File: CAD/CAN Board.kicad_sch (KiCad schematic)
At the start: 40 parts, among them J1 Conn_01x04, J10 Conn_01x03, J11 Conn_01x03, J2 Conn_01x06, J3 USB_C_Receptacle_USB2.0_16P, J4 Conn_01x02, J5 Conn_01x02, J6 Conn_01x02, J7 Conn_01x02, J8 Conn_01x02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

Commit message: updated baord
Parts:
- C1, C2: value 27p -> 15p
- Y1: value Crystal_GND24 -> 12MHz
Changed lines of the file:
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@@
 	(label "QSPI_SCLK"
 		(at 149.225 83.185 0)
-		(fields_autoplaced yes)
 		(effects
 			(font
@@
 	(label "QSPI_SD1"
 		(at 15.24 83.82 0)
-		(fields_autoplaced yes)
 		(effects
 			(font
@@
 	(label "QSPI_SS"
 		(at 149.225 80.01 0)
-		(fields_autoplaced yes)
 		(effects
 			(font
@@
 	(label "XOUT"
 		(at 15.24 116.84 0)
-		(fields_autoplaced yes)
 		(effects
 			(font
@@
 	(label "QSPI_SD3"
 		(at 15.24 88.9 0)
-		(fields_autoplaced yes)
 		(effects
 			(font
@@
 	(label "QSPI_SD0"
 		(at 195.58 75.565 180)
-		(fields_autoplaced yes)
 		(effects
 			(font
@@
 	(label "QSPI_SD2"
 		(at 195.58 83.185 180)
-		(fields_autoplaced yes)
 		(effects
 			(font
@@
 	(label "QSPI_SD2"
 		(at 15.24 86.36 0)
-		(fields_autoplaced yes)
 		(effects
 			(font
@@
 	(label "QSPI_SD3"
 		(at 195.58 85.725 180)
-		(fields_autoplaced yes)
 		(effects
 			(font
@@
 	(label "ucd+"
 		(at 90.17 66.04 0)
-		(fields_autoplaced yes)
 		(effects
 			(font
@@
 	(label "QSPI_SCLK"
 		(at 15.24 92.71 0)
-		(fields_autoplaced yes)
 		(effects
 			(font
@@
 	(label "XOUT"
 		(at 46.99 33.02 180)
-		(fields_autoplaced yes)
 		(effects
 			(font
@@
 	(label "XIN"
 		(at 15.24 111.76 0)
-		(fields_autoplaced yes)
 		(effects
 			(font
@@
 	(label "ucd-"
 		(at 90.17 68.58 0)
-		(fields_autoplaced yes)
 		(effects
 			(font
@@
 	(label "QSPI_SS"
 		(at 15.24 77.47 0)
-		(fields_autoplaced yes)
 		(effects
 			(font
@@
 	(label "QSPI_SD0"
 		(at 15.24 81.28 0)
-		(fields_autoplaced yes)
 		(effects
 			(font
@@
 	(label "QSPI_SD1"
 		(at 195.58 78.105 180)
-		(fields_autoplaced yes)
 		(effects
 			(font
@@
 	(label "XIN"
 		(at 45.72 22.86 180)
-		(fields_autoplaced yes)
 		(effects
 			(font
@@
 			)
 		)
-		(property "Value" "27p"
+		(property "Value" "15p"
 			(at 20.447 35.941 0)
 			(effects
@@
 			)
 		)
-		(property "Value" "27p"
+		(property "Value" "15p"
 			(at 20.447 25.781 0)
 			(effects
@@
 			)
 		)
-		(property "Value" "Crystal_GND24"
+		(property "Value" "12MHz"
 			(at 41.91 25.781 90)
 			(effects
@@
 			)
 		)
-		(property "Datasheet" "~"
+		(property "Datasheet" "Abracon ABM8-272-T3"
 			(at 29.21 27.94 0)
 			(effects

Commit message: added LED and cleanup
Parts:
- removed J1: Conn_01x04, Connector_Molex:Molex_PicoBlade_53047-0410_1x04_P1.25mm_Vertical, symbol Connector_Generic:Conn_01x04
- removed J10: Conn_01x03, Connector_Molex:Molex_PicoBlade_53047-0310_1x03_P1.25mm_Vertical, symbol Connector_Generic:Conn_01x03
- removed J2: Conn_01x06, Connector_Molex:Molex_PicoBlade_53047-0610_1x06_P1.25mm_Vertical, symbol Connector_Generic:Conn_01x06
- added D1: LED, LED_SMD:LED_0603_1608Metric_Pad1.05x0.95mm_HandSolder, symbol Device:LED
- added J1, J12: Conn_01x03, Connector_Molex:Molex_PicoBlade_53047-0310_1x03_P1.25mm_Vertical, symbol Connector_Generic:Conn_01x03
- added J10: Conn_01x02, Connector_Molex:Molex_PicoBlade_53047-0210_1x02_P1.25mm_Vertical, symbol Connector_Generic:Conn_01x02
- added J2: Conn_01x04, Connector_Molex:Molex_PicoBlade_53047-0410_1x04_P1.25mm_Vertical, symbol Connector_Generic:Conn_01x04
- added Q1: NMOS, Package_TO_SOT_SMD:SOT-323_SC-70, symbol Simulation_SPICE:NMOS
- added R19: 1k, Resistor_SMD:R_0603_1608Metric_Pad0.98x0.95mm_HandSolder, symbol Device:R
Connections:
- net +3V3: now also D1.2 (A), J12.2 (Pin_2)
- net +5V: now also J12.1 (Pin_1)
- net ADC 0: now also J1.2 (Pin_2)
- net ADC 1: now also J1.3 (Pin_3)
- net GND: now also J12.3 (Pin_3), Q1.3 (S)
- net GPIO 15: now also J1.1 (Pin_1), Q1.2 (G)
- net RX0: now also J10.2 (Pin_2)
- net SPI1 CSn: now also J2.3 (Pin_3)
- net SPI1 RX: now also J2.2 (Pin_2)
- net SPI1 SCK: now also J2.4 (Pin_4)
- net SPI1 TX: now also J2.1 (Pin_1)
- net TX0: now also J10.1 (Pin_1)
- new net: D1.1 (K), R19.1
- new net: Q1.1 (D), R19.2
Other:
- moved on the sheet: J11

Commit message: updated board
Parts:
- added R20: 220, Resistor_SMD:R_0603_1608Metric_Pad0.98x0.95mm_HandSolder, symbol Device:R
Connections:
- net GPIO 15: now also R20.1; no longer Q1.2 (G)
- new net: Q1.2 (G), R20.2
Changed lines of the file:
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@@
 	(global_label "GPIO 15"
 		(shape bidirectional)
-		(at 214.63 77.47 180)
+		(at 214.63 69.85 180)
 		(fields_autoplaced yes)
 		(effects
@@
 		)
 		(property "Intersheetrefs" "${INTERSHEET_REFS}"
-			(at 202.6716 77.47 0)
+			(at 202.6716 69.85 0)
 			(effects
 				(font
@@
 					(unit 1)
 				)
+			)
+		)
+	)
+	(symbol
+		(lib_id "Device:R")
+		(at 214.63 73.66 0)
+		(unit 1)
+		(exclude_from_sim no)
+		(in_bom yes)
+		(on_board yes)
+		(dnp no)
+		(fields_autoplaced yes)
+		(property "Reference" "R20"
+			(at 217.17 72.3899 0)
+			(effects
+				(font
+					(size 1.27 1.27)
+				)
+				(justify left)
+			)
+		)
+		(property "Value" "220"
+			(at 217.17 74.9299 0)
+			(effects
+				(font
+					(size 1.27 1.27)
+				)
+				(justify left)
+			)
+		)
+		(property "Footprint" "Resistor_SMD:R_0603_1608Metric_Pad0.98x0.95mm_HandSolder"
+			(at 212.852 73.66 90)
+			(effects
+				(font
+					(size 1.27 1.27)
+				)
+				(hide yes)
+			)
+		)
+		(property "Datasheet" "~"
+			(at 214.63 73.66 0)
+			(effects
+				(font
+					(size 1.27 1.27)
+				)
+				(hide yes)
+			)
+		)
+		(property "Description" "Resistor"
+			(at 214.63 73.66 0)
+			(effects
+				(font
+					(size 1.27 1.27)
+				)
+				(hide yes)
+			)
+		)
+		(pin "1"
+		)
+		(pin "2"
+		)
+		(instances
+			(project ""
+				(path "/7d82ce85-7222-412b-9514-e26c0dea1256"
+					(reference "R20")
+					(unit 1)
+				)

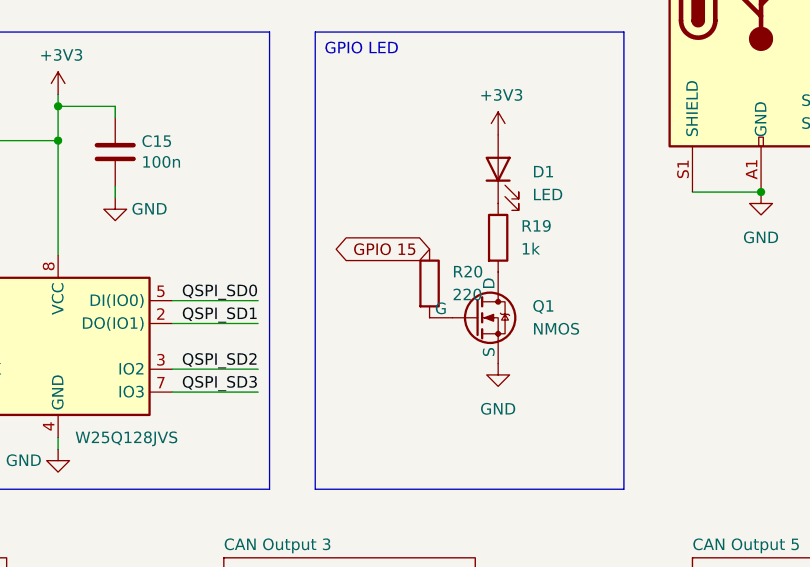
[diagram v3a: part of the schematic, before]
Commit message: updated CAN termination
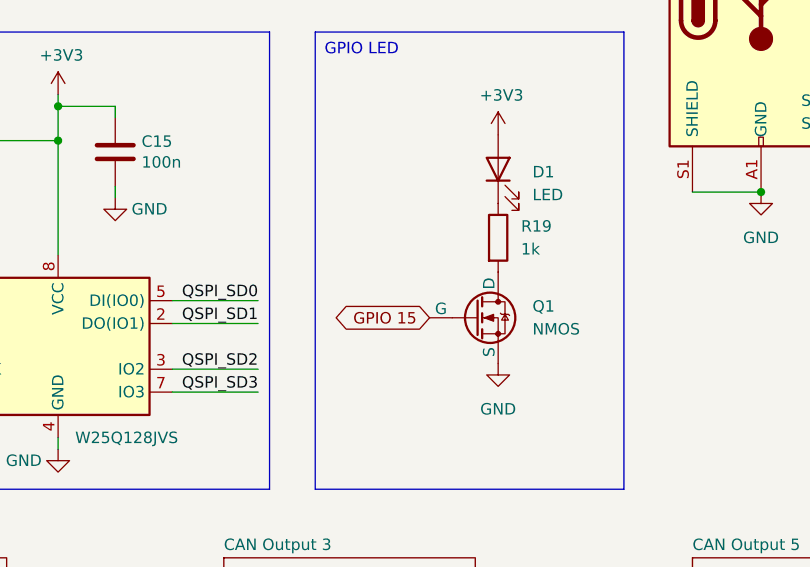
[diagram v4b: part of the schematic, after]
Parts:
- removed R20: 220, Resistor_SMD:R_0603_1608Metric_Pad0.98x0.95mm_HandSolder, symbol Device:R
- R19: footprint Resistor_SMD:R_0603_1608Metric_Pad0.98x0.95mm_HandSolder -> Resistor_SMD:R_0603_1608Metric
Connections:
- net GPIO 15: now also Q1.2 (G)
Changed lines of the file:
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@@
 	(global_label "GPIO 15"
 		(shape bidirectional)
-		(at 214.63 69.85 180)
+		(at 214.63 77.47 180)
 		(fields_autoplaced yes)
 		(effects
@@
 		)
 		(property "Intersheetrefs" "${INTERSHEET_REFS}"
-			(at 202.6716 69.85 0)
+			(at 202.6716 77.47 0)
 			(effects
 				(font
@@
 			)
 		)
-		(property "Footprint" "Resistor_SMD:R_0603_1608Metric_Pad0.98x0.95mm_HandSolder"
+		(property "Footprint" "Resistor_SMD:R_0603_1608Metric"
 			(at 220.472 68.58 90)
 			(effects
@@
 					(unit 1)
 				)
-			)
-		)
-	)
-	(symbol
-		(lib_id "Device:R")
-		(at 214.63 73.66 0)
-		(unit 1)
-		(exclude_from_sim no)
-		(in_bom yes)
-		(on_board yes)
-		(dnp no)
-		(fields_autoplaced yes)
-		(property "Reference" "R20"
-			(at 217.17 72.3899 0)
-			(effects
-				(font
-					(size 1.27 1.27)
-				)
-				(justify left)
-			)
-		)
-		(property "Value" "220"
-			(at 217.17 74.9299 0)
-			(effects
-				(font
-					(size 1.27 1.27)
-				)
-				(justify left)
-			)
-		)
-		(property "Footprint" "Resistor_SMD:R_0603_1608Metric_Pad0.98x0.95mm_HandSolder"
-			(at 212.852 73.66 90)
-			(effects
-				(font
-					(size 1.27 1.27)
-				)
-				(hide yes)
-			)
-		)
-		(property "Datasheet" "~"
-			(at 214.63 73.66 0)
-			(effects
-				(font
-					(size 1.27 1.27)
-				)
-				(hide yes)
-			)
-		)
-		(property "Description" "Resistor"
-			(at 214.63 73.66 0)
-			(effects
-				(font
-					(size 1.27 1.27)
-				)
-				(hide yes)
-			)
-		)
-		(pin "1"
-		)
-		(pin "2"
-		)
-		(instances
-			(project ""
-				(path "/7d82ce85-7222-412b-9514-e26c0dea1256"
-					(reference "R20")
-					(unit 1)
-				)
